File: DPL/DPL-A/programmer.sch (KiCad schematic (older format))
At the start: 5 parts, among them J2 Programmer, SW1 Reset_push

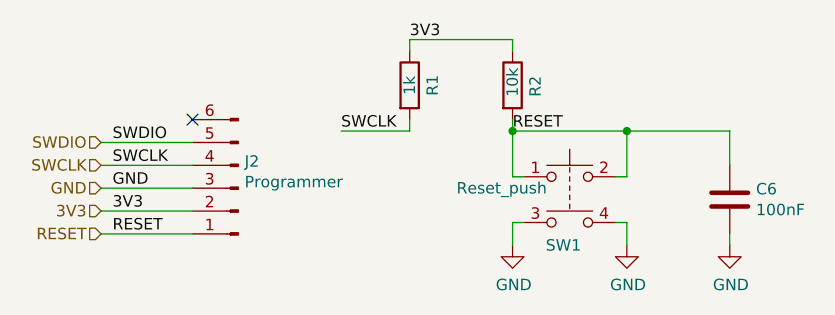
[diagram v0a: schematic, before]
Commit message: First prototype of the interstage-balloon release system type A.
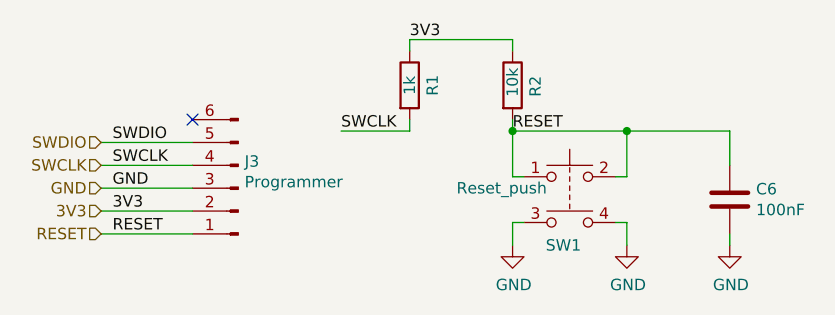
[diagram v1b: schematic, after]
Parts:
- renumbered J2 to J3
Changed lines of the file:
@@
 $EndComp
 $Comp
-L Connector:Conn_01x06_Male J2
+L Connector:Conn_01x06_Male J3
 U 1 1 5E278DB4
 P 5450 2800
-F 0 "J2" H 5422 2683 50  0000 R CNN
+F 0 "J3" H 5422 2683 50  0000 R CNN
 F 1 "Programmer" H 5422 2773 50  0000 R CNN
 F 2 "Connector_Molex:Molex_PicoBlade_53048-0610_1x06_P1.25mm_Horizontal" H 5450 2800 50  0001 C CNN
